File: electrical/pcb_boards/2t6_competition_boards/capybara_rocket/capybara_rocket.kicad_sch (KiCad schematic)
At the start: 53 parts, among them J1 SparkFun MAX-M10S, J10 Wurth_M4_62000411622, J11 Wurth_M4_62000411622, J12 Wurth_M3_62000311622, J13 Wurth_M3_62000311622, J14 Wurth_M3_62000311622, J15 Wurth_M3_62000311622, J16 Wurth_M3_62000311622, J17 Wurth_M3_62000311622, J2 VL53L1-SATEL, J3 Wurth_M2_62000211622, J4 Wurth_M2_62000211622, J5 Wurth_M2_62000211622, J6 Wurth_M2_62000211622, J7 Wurth_M2_62000211622, J9 Wurth_M4_62000411622, U1 WRL-11812, U10 MAX756CPA_, U11 LTC3536EMSE_PBF, U12 MP3414AGJ-Z, U13 Adafruit BMP581, U14 INA219BIDR, U2 Adafruit BNO085, U4 STM32 NUCLEO-G431KB, U5 DS1307+, U6 NE555P, U7 25LC1024-E/P, U8 DRV8212DRLR, U9 SN74LVC1G04DBVR, Y1 AB38T-32.768KHZ

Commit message: Adding BMP581 KiCad models and big boi updates to CPL PCB
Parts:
- removed J11: Wurth_M4_62000411622, RSX_CanSat_Custom_KiCad_Footprints:J_Wurth_WR-WTB_62000411622, symbol RSX_CanSat_Custom_KiCad_Symbols:Wurth_M4_62000411622
- removed U13: Adafruit BMP581, RSX_CanSat_Custom_KiCad_Footprints:Adafruit_BMP581, symbol RSX_CanSat_Custom_KiCad_Symbols:Adafruit_BMP581
- added J16: DC Motor, RSX_CanSat_Custom_KiCad_Footprints:J_Wurth_WR-WTB_62000411622, symbol RSX_CanSat_Custom_KiCad_Symbols:Wurth_M4_62000411622
- added R10, R5, R6, R8, R9: 100Ω, Resistor_SMD:R_0603_1608Metric_Pad0.98x0.95mm_HandSolder, symbol Device:R
- added U4: Adafruit BMP581, RSX_CanSat_Custom_KiCad_Footprints:Adafruit_BMP581, symbol RSX_CanSat_Custom_KiCad_Symbols:Adafruit_BMP581
- J10: renamed from J12; value Wurth_M3_62000311622 -> Servo NC
- J11: renamed from J13; value Wurth_M3_62000311622 -> Servo CC
- J12: renamed from J14; value Wurth_M3_62000311622 -> Servo EGG
- J13: renamed from J15; value Wurth_M3_62000311622 -> Servo ELEVATOR
- J14: renamed from J16; value Wurth_M3_62000311622 -> Servo AILERON 1
- J15: renamed from J17; value Wurth_M3_62000311622 -> Servo AILERON 2
- J3: value Wurth_M2_62000211622 -> LED
- J7: renamed from J9; value Wurth_M4_62000411622 -> Ground Camera
- J8: renamed from J10; value Wurth_M4_62000411622 -> Payload Camera
- U5: renamed from U14; value INA219BIDR -> INA219
- U6: renamed from U7; value 25LC1024-E/P -> EEPROM
- U8: renamed from U1; value WRL-11812 -> SparkFun XBee Explorer
- renumbered C3 to C2, C2 to C3, J4 to J1, J5 to J2, J6 to J4, J7 to J5, J2 to J6, J1 to J9, R3 to R1, R5 to R11, R6 to R12, R1 to R3, U6 to U1, U8 to U10, U10 to U11, U11 to U12, U12 to U13, U5 to U2, U2 to U3, U4 to U7
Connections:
- net 3.3V: now also J6.4, R7.1, U5.7 (VIN-), U6.7 (*HOLD), U6.8 (VCC), U4.1 (VIN); no longer J6.2
- net 5V: now also J10.3, J11.3, J12.3, J13.3, J14.3, J15.3, J7.4, J8.4, J16.4
- net AILERON: now also J14.2, J15.2
- net CC_REL: now also J11.2
- net CS: now also U6.1 (*CS)
- net EGG_REL: now also J12.2
- net ELEVATOR: now also J13.2
- net GND: now also D1.1 (K), D2.1 (K), D3.1 (K), D4.1 (K), D5.1 (K), J10.1, J11.1, J12.1, J13.1, J14.1, J15.1, J7.1, J8.1, U6.3 (*WP), U6.4 (VSS), J16.1, U4.3 (GND)
- net G_CAM_IN: now also J7.2
- net G_CAM_OUT: now also J7.3
- net MISO: now also U6.2 (SO)
- net MOSI: now also U6.5 (SI)
- net NC_REL: now also J10.2
- net PG_CAM_IN: now also J8.2
- net PG_CAM_OUT: now also J8.3
- net SCL: now also J6.3, U4.4 (SCL); no longer J6.4
- net SCLK: now also U6.6 (SCK)
- net SDA: now also J6.2, U4.6 (SDA); no longer J6.3
- net WING_DIR: now also J16.3
- net WING_PWM: now also J16.2
- net at D1.2 (A): now also R5.1
- net at D3.2 (A): now also R8.1
- net at D2.2 (A): now also R6.1
- net at D5.2 (A): now also R10.1
- net at D4.2 (A): now also R9.1
- no-connect marks 33 -> 34
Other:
- note added: "EEPROM Circuit"
- moved on the sheet: C5, C6, D1, D2, D3, D4, D5, J10, J11, J12, J13, J14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

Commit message: March 15 CPL PCB update
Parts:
- J1: value Wurth_M2_62000211622 -> 3.6V Battery
- J10: renamed from J13; value Servo ELEVATOR -> Elevator
- J12: renamed from J14; value Servo AILERON 1 -> Aileron 1
- J13: renamed from J15; value Servo AILERON 2 -> Aileron 2
- J2: renamed from J4; value Wurth_M2_62000211622 -> 1.2V Battery
- J3: renamed from J2; value Wurth_M2_62000211622 -> 3.6V Switch
- J4: renamed from J5; value Wurth_M2_62000211622 -> 1.2V Switch
- J6: renamed from J10; value Servo NC -> NC
- J7: renamed from J11; value Servo CC -> CC
- J9: renamed from J12; value Servo EGG -> Egg
- renumbered J9 to J11, J7 to J14, J16 to J15, J8 to J16, J3 to J5, J6 to J8, R8 to R10, R9 to R11, R10 to R12, R7 to R5, R11 to R6, R12 to R7, R5 to R8, R6 to R9, U11 to U10, U6 to U11, U7 to U12, U8 to U13, U10 to U4, U9 to U5, U4 to U6, U12 to U7, U13 to U8, U5 to U9
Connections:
- net 3.6V is gone; now on net +3.6V: R5.2, U9.8 (VIN+)
- net +1.2V: now also J2.2, J4.2
- net +3.6V: now also J1.2, J3.2
- net 3.3V: now also R4.2
- net 5V: no longer J1.1, J3.1
- net GND: now also J1.1, J2.1, J3.1, J4.1, J5.1; no longer J1.2, J3.2, J5.2
- net at R4.1: now also J5.2; no longer J5.1
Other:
- note added: "Battery Input & Control Circuits"
- note added: "CPL LED Circuit"
- note added: "Camera Circuits"
- note added: "I2C Pull-Up Circuits"
- note added: "Servo Circuits"
- note removed: "I2C Pull-Up Circuit"
- note removed: "Power Management"
- moved on the sheet: C7, D1, D2, D3, D4, D5, J1, J10, J11, J12, J13, J14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

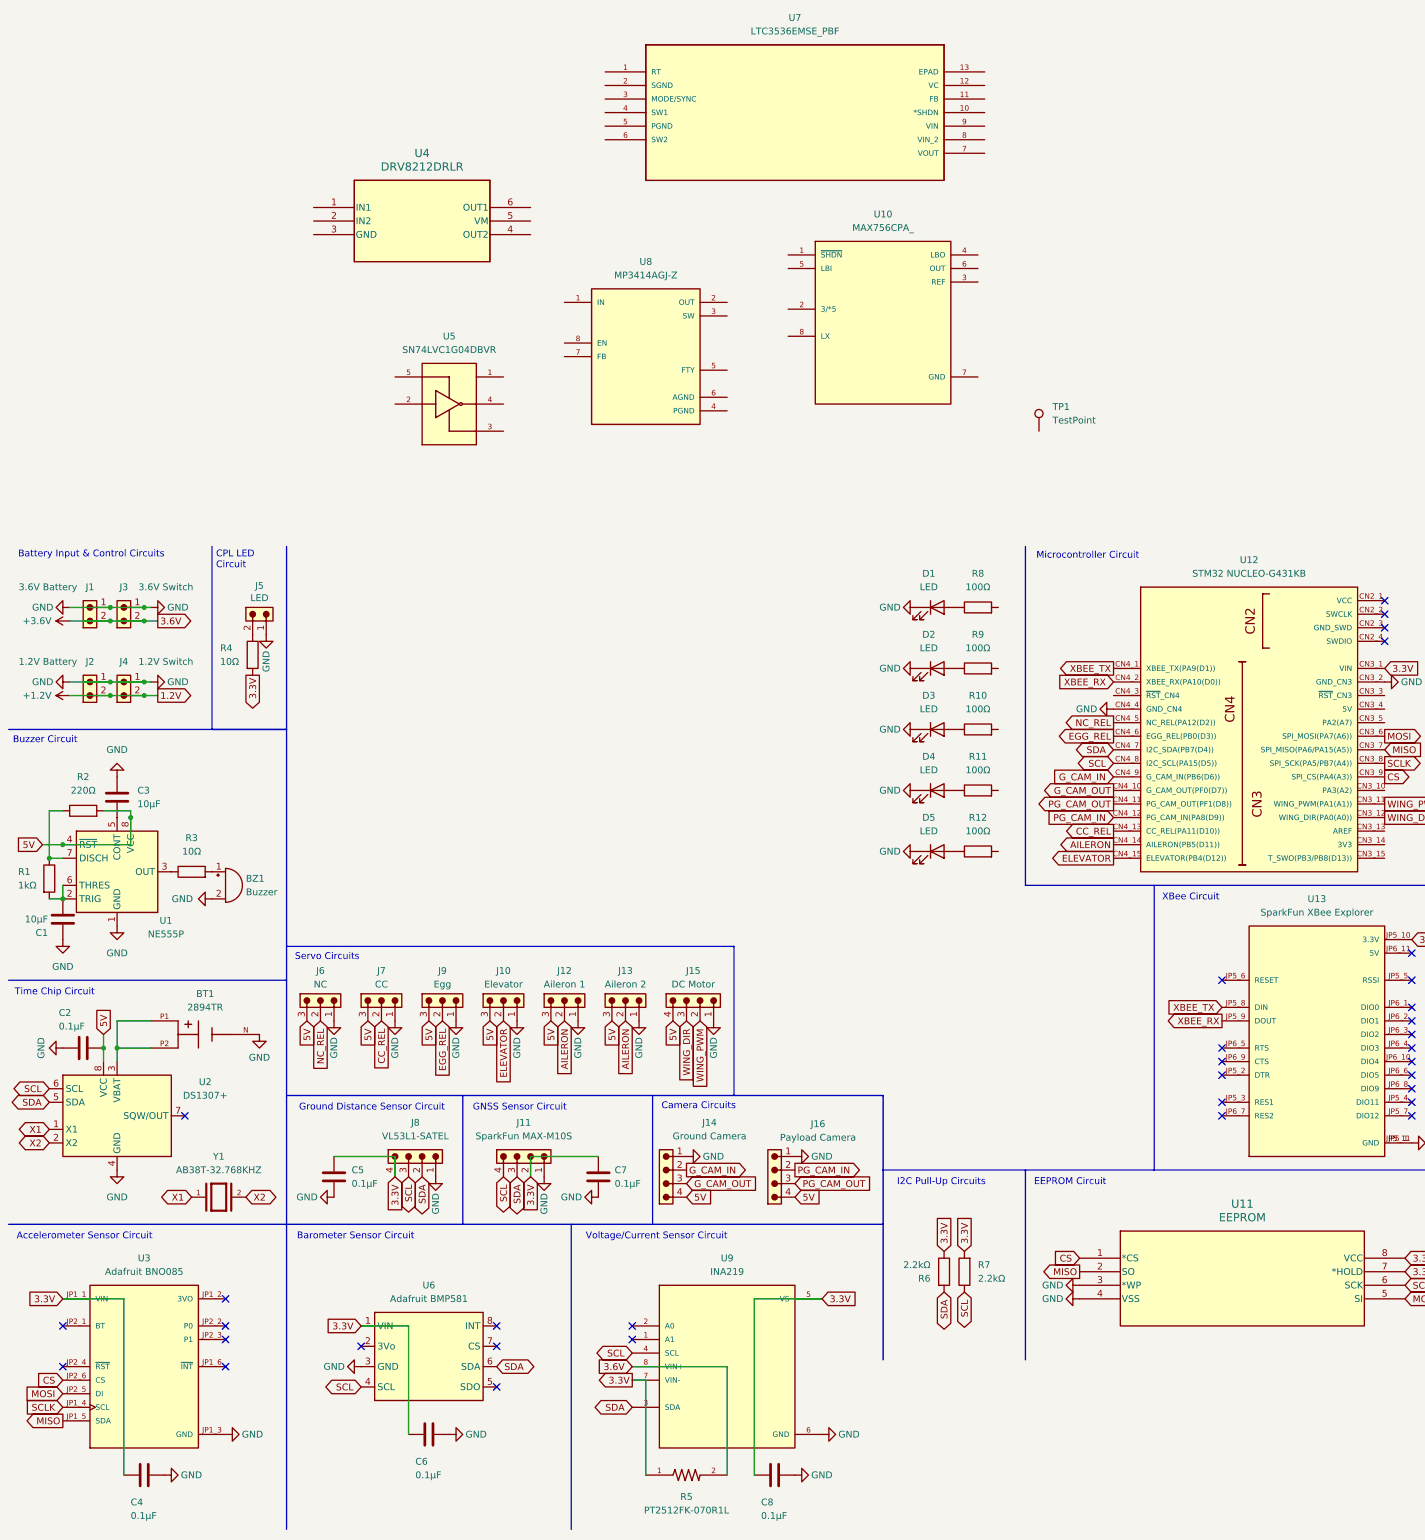
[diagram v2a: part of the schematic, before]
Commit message: LT3536 and MP3414 circuit design
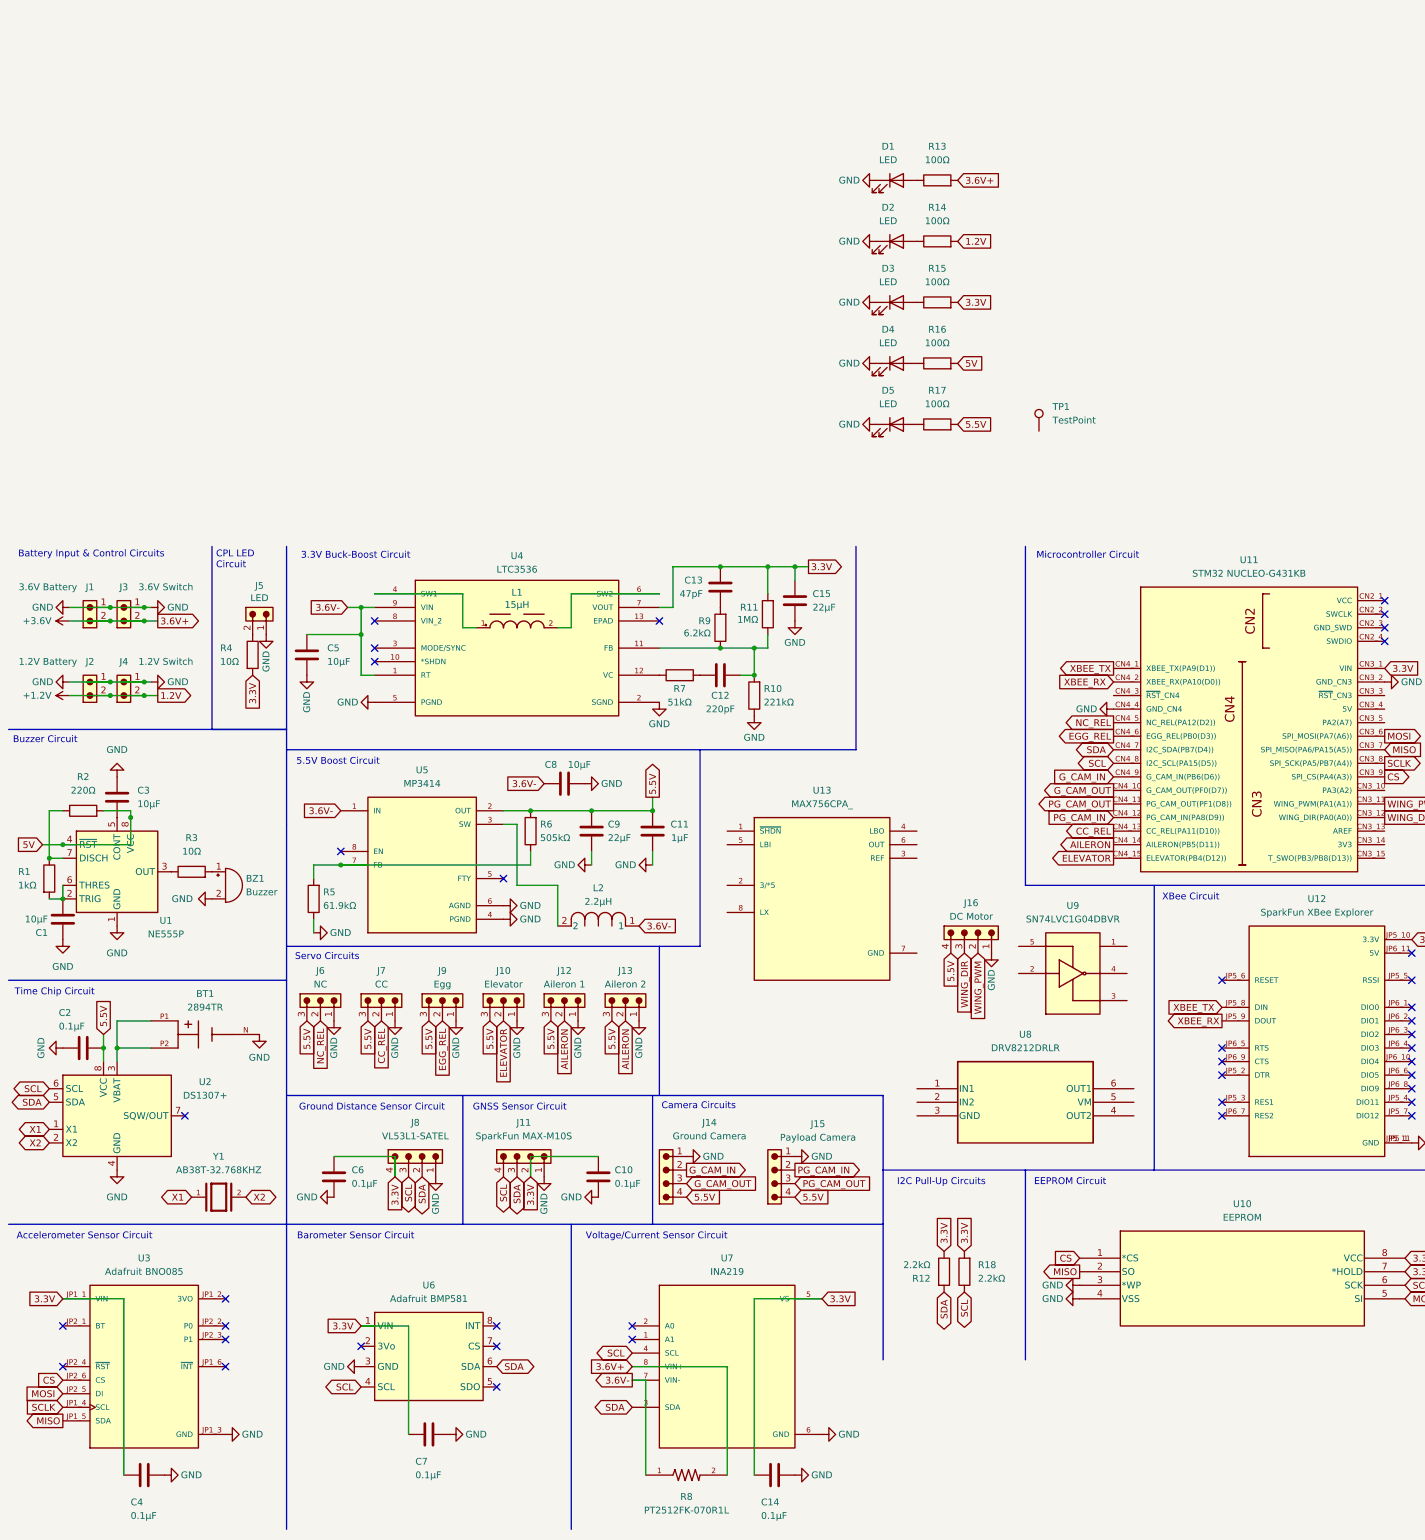
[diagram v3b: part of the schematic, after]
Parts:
- added C11: 1μF, Capacitor_SMD:C_0402_1005Metric_Pad0.74x0.62mm_HandSolder, symbol Device:C
- added C12: 220pF, Capacitor_SMD:C_0805_2012Metric_Pad1.18x1.45mm_HandSolder, symbol Device:C
- added C13: 47pF, Capacitor_SMD:C_0603_1608Metric_Pad1.08x0.95mm_HandSolder, symbol Device:C
- added C15, C9: 22μF, Capacitor_SMD:C_0805_2012Metric_Pad1.18x1.45mm_HandSolder, symbol Device:C
- added C5, C8: 10μF, Capacitor_SMD:C_1206_3216Metric_Pad1.33x1.80mm_HandSolder, symbol Device:C
- added L1: 15μH, RSX_CanSat_Custom_KiCad_Footprints:WE-TPC_4828, symbol RSX_CanSat_Custom_KiCad_Symbols:WE-TPC_4828
- added L2: 2.2μH, IND_BOURNS_SRN6045, symbol RSX_CanSat_Custom_KiCad_Symbols:SRN6045-2R2Y
- added R10: 221kΩ, Resistor_THT:R_Axial_DIN0207_L6.3mm_D2.5mm_P7.62mm_Horizontal, symbol Device:R
- added R11: 1MΩ, Resistor_THT:R_Axial_DIN0207_L6.3mm_D2.5mm_P7.62mm_Horizontal, symbol Device:R
- added R5: 61.9kΩ, Resistor_SMD:R_1206_3216Metric_Pad1.30x1.75mm_HandSolder, symbol Device:R
- added R6: 505kΩ, Resistor_SMD:R_0603_1608Metric_Pad0.98x0.95mm_HandSolder, symbol Device:R
- added R7: 51kΩ, Resistor_SMD:R_0603_1608Metric_Pad0.98x0.95mm_HandSolder, symbol Device:R
- added R9: 6.2kΩ, Resistor_SMD:R_0603_1608Metric_Pad0.98x0.95mm_HandSolder, symbol Device:R
- U4: renamed from U7; value LTC3536EMSE_PBF -> LTC3536
- U5: renamed from U8; value MP3414AGJ-Z -> MP3414
- renumbered C7 to C10, C8 to C14, C5 to C6, C6 to C7, J16 to J15, J15 to J16, R6 to R12, R8 to R13, R9 to R14, R10 to R15, R11 to R16, R12 to R17, R7 to R18, R5 to R8, U11 to U10, U12 to U11, U13 to U12, U10 to U13, U9 to U7, U4 to U8, U5 to U9
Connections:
- net +1.2V: now also R14.2
- net +3.6V: now also R13.2
- net 3.3V: now also R15.2, U4.7 (VOUT), C13.2, C15.2, R11.2; no longer R8.1, U7.7 (VIN-)
- net 5V: now also R16.2; no longer C2.1, J10.3, J12.3, J13.3, J14.4, J15.4, J16.4, J6.3, J7.3, J9.3, U2.8 (VCC)
- net GND: now also U4.2 (SGND), U4.5 (PGND), U5.4 (PGND), U5.6 (AGND), C11.2, C15.1, C5.2, C8.1, C9.2, R10.1, R5.1
- net 3.6V-: now reaches U5.1 (IN)
- net 3.6V-: now also R8.1, U4.1 (RT), U4.9 (VIN), U7.7 (VIN-), C5.1, C8.2, L2.1
- net 5.5V: now reaches U5.2 (OUT)
- net 5.5V: now also C2.1, J10.3, J12.3, J13.3, J14.4, J15.4, J16.4, J6.3, J7.3, J9.3, R17.2, U2.8 (VCC), C11.1, C9.1, R6.2
- net at U5.3 (SW): now also L2.2
- net at U5.7 (FB): now also R5.2, R6.1
- net at U4.11 (FB): now also C12.1, R10.2, R11.1, R9.1
- net at U4.12 (VC): now also R7.1
- net at U4.4 (SW1): now also L1.1
- net at U4.6 (SW2): now also L1.2
- new net: C12.2, R7.2
- new net: C13.1, R9.2
- no-connect marks 34 -> 40
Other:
- note added: "3.3V Buck-Boost Circuit"
- note added: "5.5V Boost Circuit"
- moved on the sheet: D1, D2, D3, D4, D5, J16, R13, R14, R15, R16, R17, U13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

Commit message: MAX756 circuit design
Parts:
- added C16: 150μF, Capacitor_THT:CP_Radial_D6.3mm_P2.50mm, symbol Device:C_Polarized
- added C17: 100μF, Capacitor_THT:CP_Radial_D8.0mm_P3.50mm, symbol Device:C_Polarized
- added D6: 1N5820, Diode_THT:D_DO-201AD_P15.24mm_Horizontal, symbol Diode:1N5820
- added L3: 22μH, RSX_CanSat_Custom_KiCad_Footprints:IND_CD54_SUM, symbol RSX_CanSat_Custom_KiCad_Symbols:CD54NP-220MC
- U13: value MAX756CPA_ -> MAX756CPA+
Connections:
- net +1.2V: now also R17.2, U13.5 (LBI), C16.1, L3.2; no longer R14.2
- net +3.6V: now also R16.2; no longer R13.2
- net 5.5V: now also R13.2; no longer R17.2
- net 5V: now also R14.2; no longer R16.2
- net GND: now also U13.7 (GND), C16.2, C17.2
- net at U13.6 (OUT): now also C17.1, D6.1 (K)
- net at U13.8 (LX): now also D6.2 (A), L3.1
- no-connect marks 40 -> 44
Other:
- note added: "5V Boost Circuit"
- note added: "LED Indicator Circuits"
- moved on the sheet: D1, D2, D3, D4, D5, J16, R13, R14, R15, R16, R17, U13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
